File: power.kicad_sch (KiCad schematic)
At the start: 49 parts, among them Q2 MMBT5551L, Q3 STN93003, U2 XL7005A, U3 ICW6215, U4 LM1117DT-3.3, X5 PWRBTN, X6 12V OUTLET, X7 5V OUTLET

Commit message: Minors, annotation
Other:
- note added: "91k for 134v"
- title: (none) -> RedShift-117.6-LogicBoard-F103
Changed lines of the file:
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@@
 (kicad_sch (version 20230121) (generator eeschema)
   (paper "A4")
+  (title_block
+    (title "RedShift-117.6-LogicBoard-F103")
+    (date "08.12.2023")
+    (rev "0.1")
+  )
   (junction (at 85.09 38.1) (diameter 0) (color 0 0 0 0)
   )
@@
   )
   (text "VBATT > > > 12V" (at 86.36 146.05 0)
+    (effects (font (size 1.27 1.27)) (justify left bottom))
+  )
+  (text "91k for 134v" (at 99.06 40.64 0)
     (effects (font (size 1.27 1.27)) (justify left bottom))
   )
@@
   (symbol (lib_id "power:PWR_FLAG") (at 137.16 29.21 0) (unit 1)
     (in_bom yes) (on_board yes) (dnp no) (fields_autoplaced)
-    (property "Reference" "#FLG07" (at 137.16 27.305 0)
+    (property "Reference" "#FLG05" (at 137.16 27.305 0)
       (effects (font (size 1.27 1.27)) hide)
     )
@@
       (project "ShiftWay_f103"
         (path "/c57bc97c-1c43-4bb1-9424-fed846030b7b/26a2c67c-0b98-4594-97f4-678ce34d1b61"
-          (reference "#FLG07") (unit 1)
+          (reference "#FLG05") (unit 1)
         )
       )
@@
         (path "/c57bc97c-1c43-4bb1-9424-fed846030b7b/26a2c67c-0b98-4594-97f4-678ce34d1b61"
           (reference "TP4") (unit 1)
-        )
-        (path "/c57bc97c-1c43-4bb1-9424-fed846030b7b/013bb254-f239-4c32-8f76-0a97895c10b6"
-          (reference "TP?") (unit 1)
         )
       )
@@
   (symbol (lib_id "power:PWR_FLAG") (at 237.49 86.36 180) (unit 1)
     (in_bom yes) (on_board yes) (dnp no) (fields_autoplaced)
-    (property "Reference" "#FLG05" (at 237.49 88.265 0)
+    (property "Reference" "#FLG06" (at 237.49 88.265 0)
       (effects (font (size 1.27 1.27)) hide)
     )
@@
       (project "ShiftWay_f103"
         (path "/c57bc97c-1c43-4bb1-9424-fed846030b7b/26a2c67c-0b98-4594-97f4-678ce34d1b61"
-          (reference "#FLG05") (unit 1)
+          (reference "#FLG06") (unit 1)
         )
       )
@@
           (reference "TP2") (unit 1)
         )
-        (path "/c57bc97c-1c43-4bb1-9424-fed846030b7b/013bb254-f239-4c32-8f76-0a97895c10b6"
-          (reference "TP?") (unit 1)
-        )
       )
     )
@@
   (symbol (lib_id "power:PWR_FLAG") (at 237.49 86.36 180) (unit 1)
     (in_bom yes) (on_board yes) (dnp no) (fields_autoplaced)
-    (property "Reference" "#FLG06" (at 237.49 88.265 0)
+    (property "Reference" "#FLG07" (at 237.49 88.265 0)
       (effects (font (size 1.27 1.27)) hide)
     )
@@
       (project "ShiftWay_f103"
         (path "/c57bc97c-1c43-4bb1-9424-fed846030b7b/26a2c67c-0b98-4594-97f4-678ce34d1b61"
-          (reference "#FLG06") (unit 1)
+          (reference "#FLG07") (unit 1)
         )
       )
@@
           (reference "TP3") (unit 1)
         )
-        (path "/c57bc97c-1c43-4bb1-9424-fed846030b7b/013bb254-f239-4c32-8f76-0a97895c10b6"
-          (reference "TP?") (unit 1)
-        )
-      )
+      )

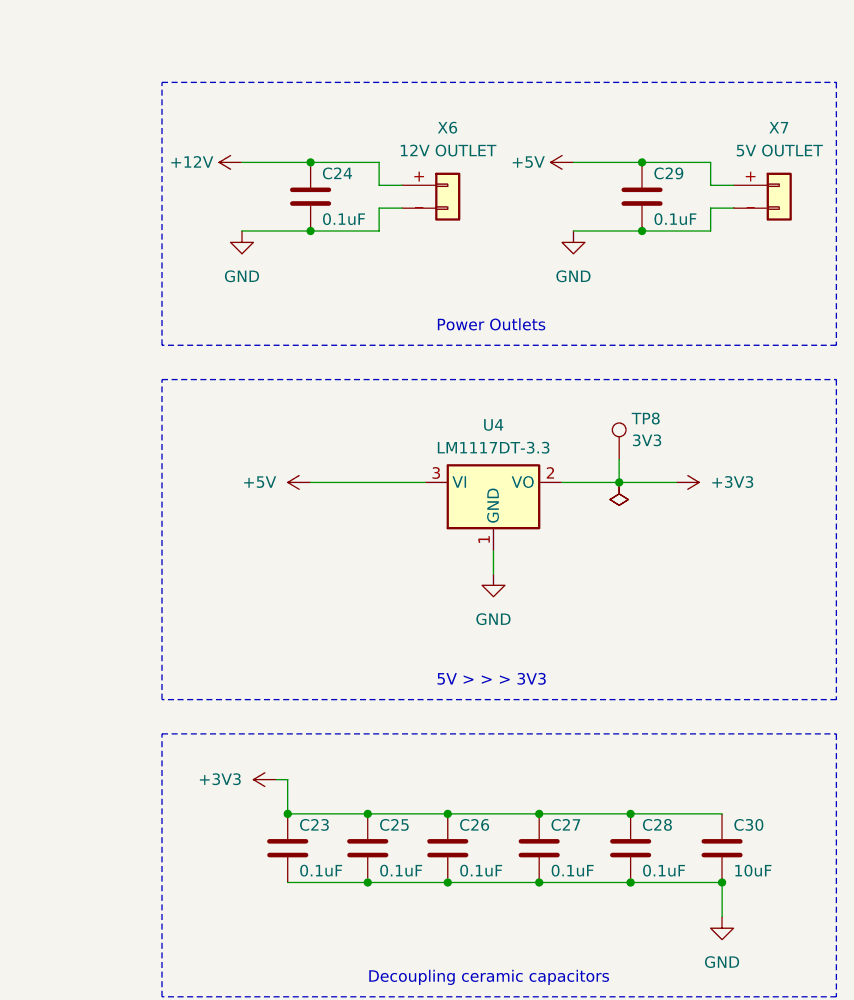
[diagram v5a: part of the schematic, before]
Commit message: Add footprints, fixed xtal
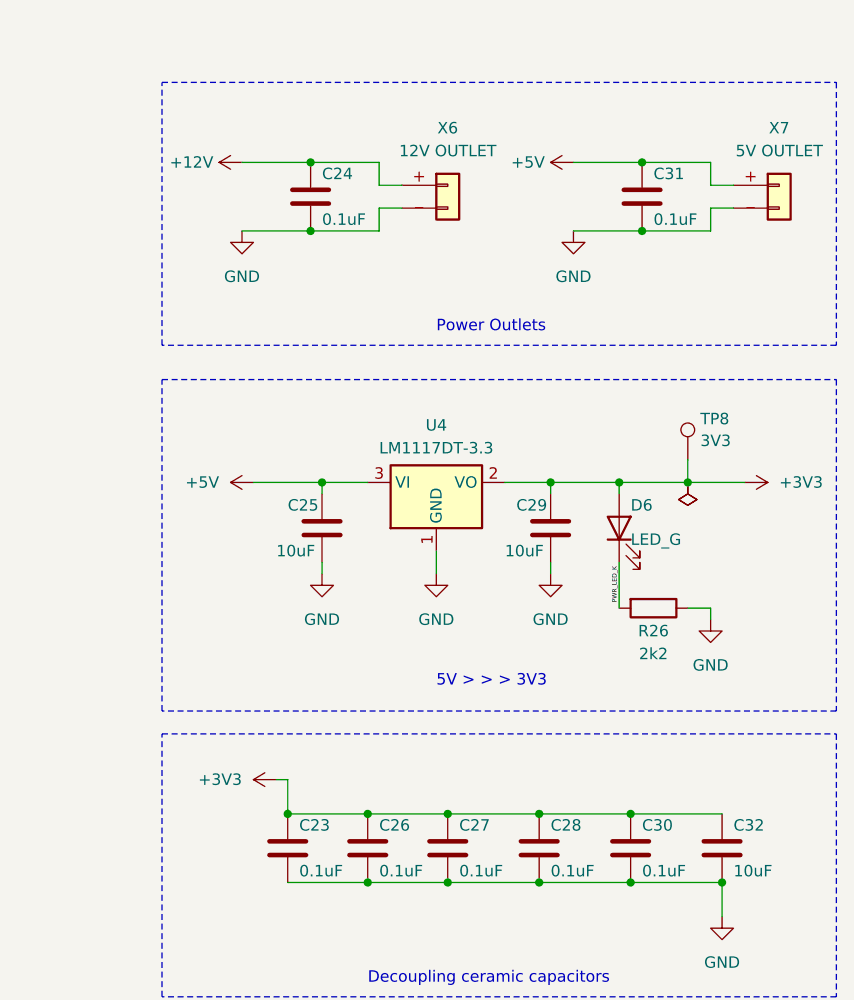
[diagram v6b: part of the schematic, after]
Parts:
- added C25: 10uF, Capacitor_SMD:C_0603_1608Metric_Pad1.08x0.95mm_HandSolder, symbol Device:C
- added C29: 10uF, Capacitor_SMD:C_0805_2012Metric, symbol Device:C
- added D6: LED_G, LED_SMD:LED_0603_1608Metric, symbol Device:LED
- added R26: 2k2, Resistor_SMD:R_0402_1005Metric, symbol Device:R
- BTN2, L1, L2: footprint (none) -> Button_Switch_SMD:SW_SPST_SKQG_WithoutStem
- C15: footprint (none) -> Capacitor_SMD:CP_Elec_10x10
- C16, C17, C22: footprint Capacitor_SMD:C_0402_1005Metric -> Capacitor_SMD:C_0805_2012Metric_Pad1.18x1.45mm_HandSolder
- C18: footprint (none) -> Capacitor_SMD:C_0805_2012Metric_Pad1.18x1.45mm_HandSolder
- C19: footprint (none) -> Capacitor_SMD:C_0603_1608Metric_Pad1.08x0.95mm_HandSolder
- C20: footprint (none) -> Capacitor_SMD:CP_Elec_6.3x7.7
- C21: footprint (none) -> Capacitor_SMD:CP_Elec_10x10.5
- C23, C24: footprint Capacitor_SMD:C_0402_1005Metric -> Capacitor_SMD:C_0603_1608Metric_Pad1.08x0.95mm_HandSolder
- C26: renamed from C25; footprint Capacitor_SMD:C_0402_1005Metric -> Capacitor_SMD:C_0603_1608Metric_Pad1.08x0.95mm_HandSolder
- C27: renamed from C26; footprint Capacitor_SMD:C_0402_1005Metric -> Capacitor_SMD:C_0603_1608Metric_Pad1.08x0.95mm_HandSolder
- C28: renamed from C27; footprint Capacitor_SMD:C_0402_1005Metric -> Capacitor_SMD:C_0603_1608Metric_Pad1.08x0.95mm_HandSolder
- C30: renamed from C28; footprint Capacitor_SMD:C_0402_1005Metric -> Capacitor_SMD:C_0603_1608Metric_Pad1.08x0.95mm_HandSolder
- C31: renamed from C29; footprint Capacitor_SMD:C_0402_1005Metric -> Capacitor_SMD:C_0603_1608Metric_Pad1.08x0.95mm_HandSolder
- C32: renamed from C30; footprint Capacitor_SMD:C_0603_1608Metric -> Capacitor_SMD:C_0603_1608Metric_Pad1.08x0.95mm_HandSolder
- D4: footprint (none) -> Capacitor_SMD:C_Elec_6.3x7.7
- R15: footprint (none) -> Resistor_SMD:R_2010_5025Metric_Pad1.40x2.65mm_HandSolder
- R16, R17, R18, R19, R20, R21, R22, R23, R24, R25: footprint (none) -> Resistor_SMD:R_0603_1608Metric_Pad0.98x0.95mm_HandSolder
- TP2, TP3, TP4, TP5, TP6, TP7, TP8: footprint (none) -> TestPoint:TestPoint_Pad_D2.0mm
- U2, U3: footprint (none) -> Package_SO:SOP-8_3.9x4.9mm_P1.27mm
- XP1: footprint (none) -> Connector_AMASS:AMASS_XT30PW-M_1x02_P2.50mm_Horizontal
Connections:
- net +3V3: now also C29.1, D6.2 (A)
- net +5V: now also C25.1
- net GND: now also C25.2, C29.2, R26.1
- new net PWR_LED_K: D6.1 (K), R26.2
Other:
- moved on the sheet: TP8, U4

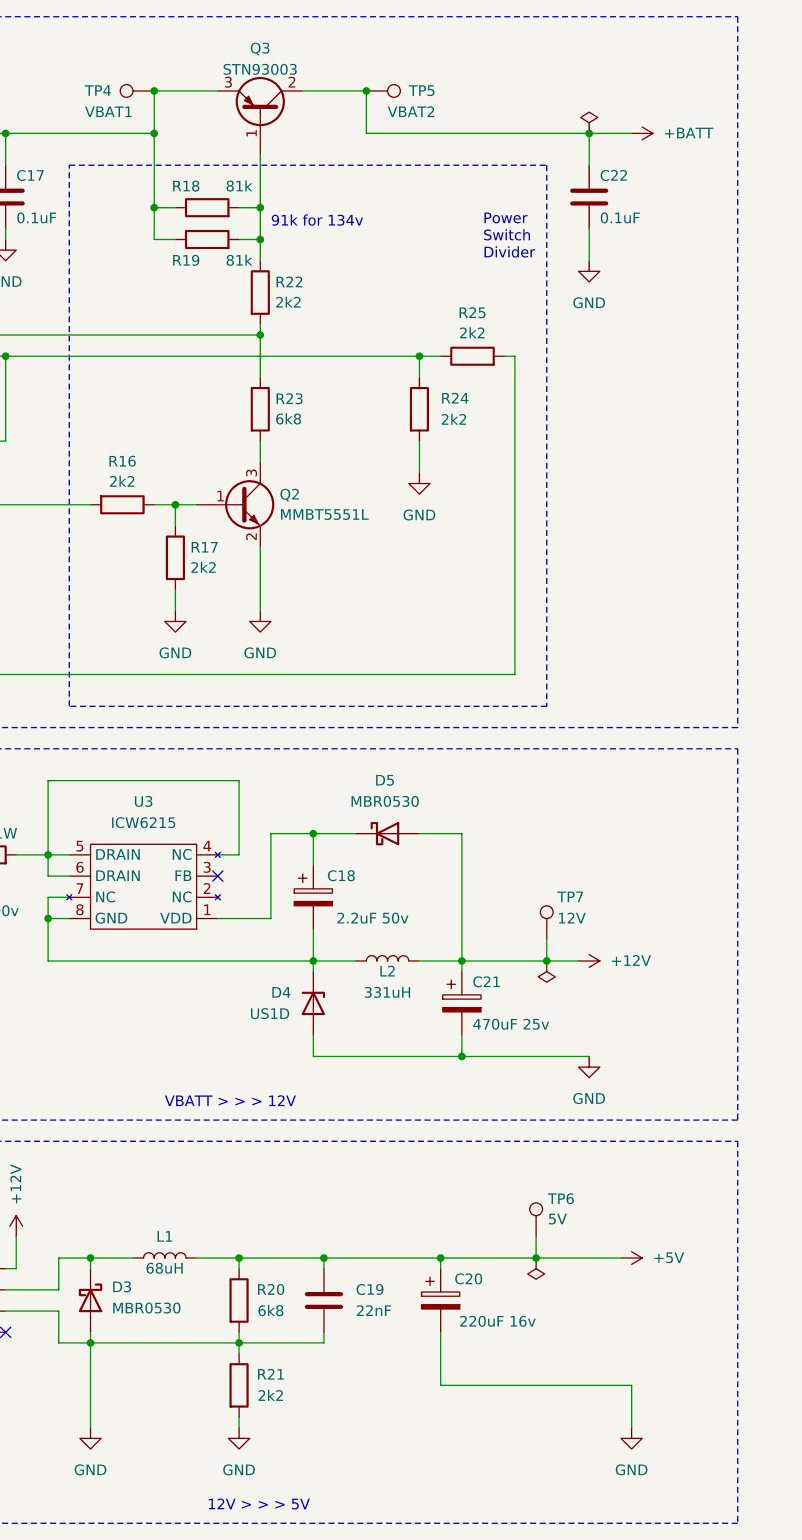
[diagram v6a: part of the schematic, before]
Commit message: Add files via upload
Add leds and minors
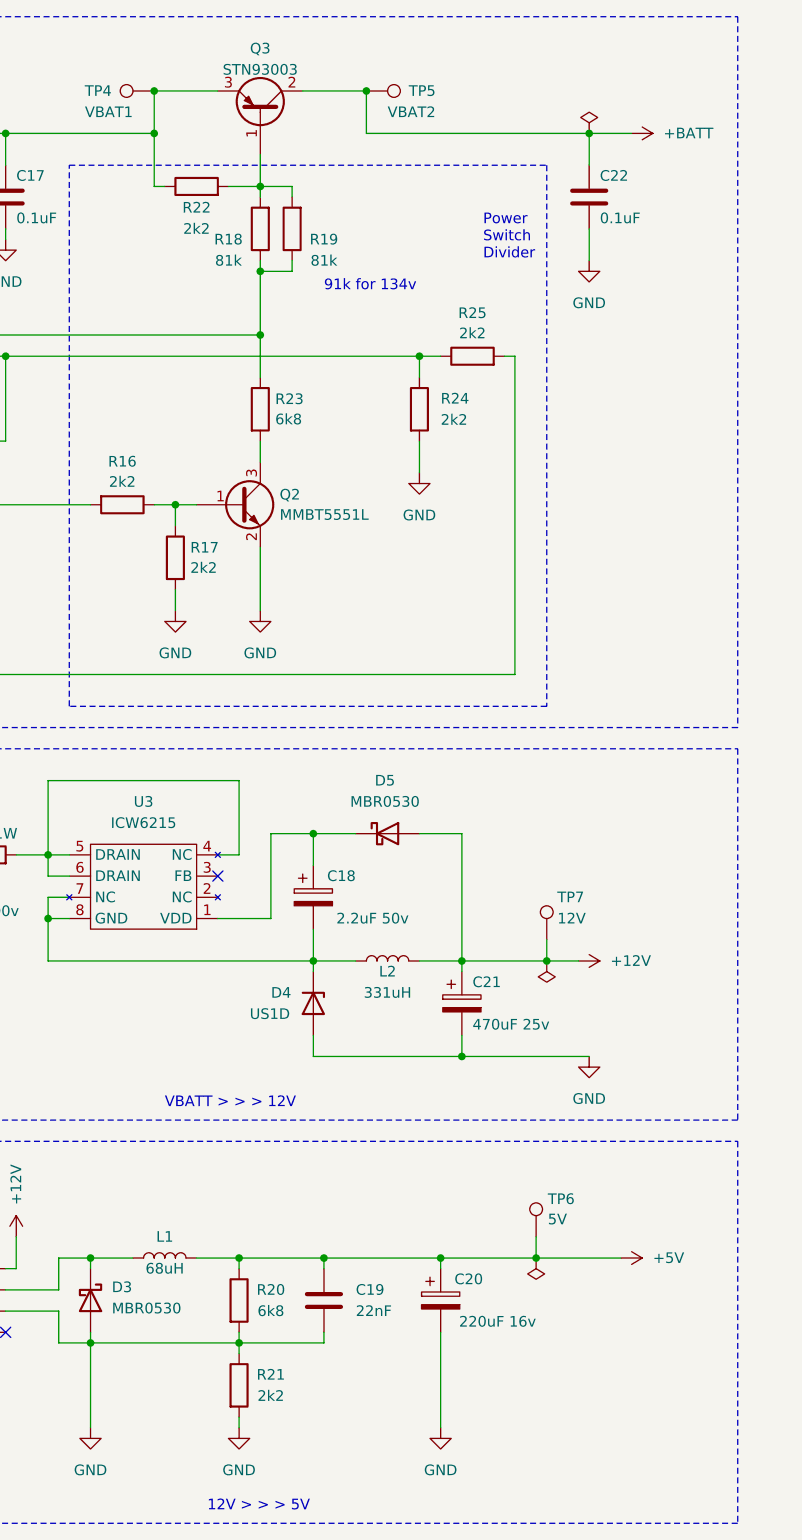
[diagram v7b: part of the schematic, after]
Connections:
- net at BTN2.1, R23.1, X5.+ (Pin_1): now also R18.1, R19.1; no longer R22.2
- net at C16.1, C17.1, Q3.3 (E)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: now also R22.1; no longer R18.1, R19.1
- net at Q3.1 (B), R18.2, R19.2: now also R22.2; no longer R22.1

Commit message: fixed some footprints
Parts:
- removed D4: US1D, Capacitor_SMD:C_Elec_6.3x7.7, symbol Device:D_Zener
- added D5: US1D, Diode_SMD:D_SMA, symbol Diode:US1D
- L1: footprint Button_Switch_SMD:SW_SPST_SKQG_WithoutStem -> Inductor_SMD:L_Bourns_SRP7028A_7.3x6.6mm
- L2: footprint Button_Switch_SMD:SW_SPST_SKQG_WithoutStem -> Inductor_SMD:L_Bourns_SRR1208_12.7x12.7mm
- renumbered D3 to D4, D5 to D6, D6 to D7, R22 to R18, R20 to R19, R21 to R20, R18 to R21, R23 to R22, R19 to R23, X5 to X6, X6 to X7, X7 to X8
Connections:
- net GND: now also D5.2 (A)
- net at C18.2, L2.1, U3.7 (NC)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: now also D5.1 (K)
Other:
- moved on the sheet: L2, TP7
